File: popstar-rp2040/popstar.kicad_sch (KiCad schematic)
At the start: 31 parts, among them J1 JST SH 4-pin, J2 SWD, SW1 Boot, U1 RP2040, U2 XC6206PxxxMR, U3 SRV05-4, U4 W25Q128JVS, Y1 12MHz

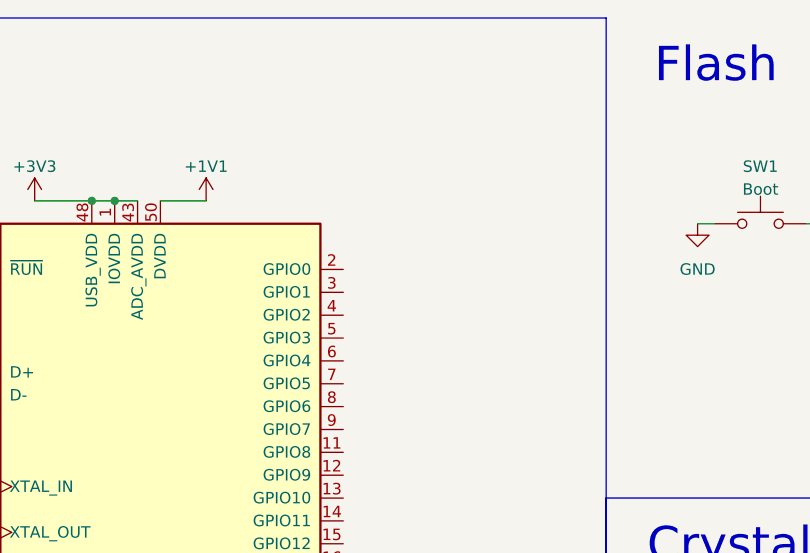
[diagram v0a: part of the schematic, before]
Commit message: Cleaned up LED schematic impl.
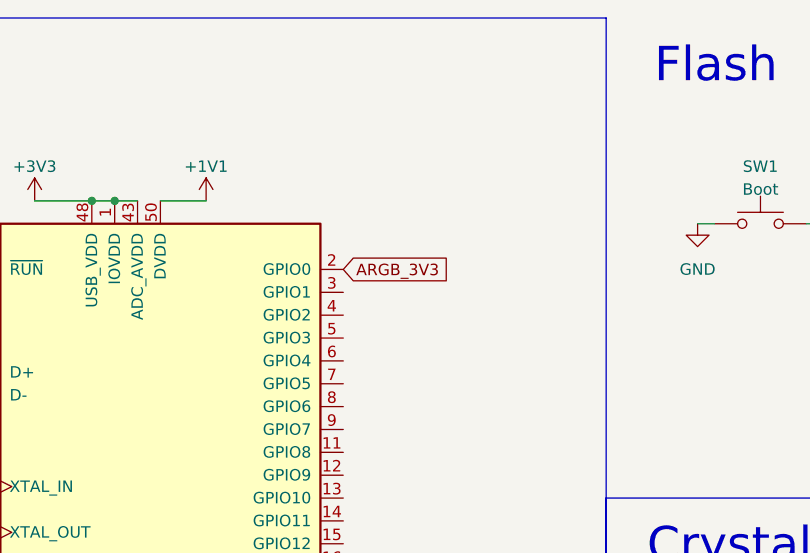
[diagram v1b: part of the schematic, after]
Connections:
- net ARGB_3V3: now reaches U1.2 (GPIO0)
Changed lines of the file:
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@@
+    )
+  )
+  (global_label "ARGB_3V3" (shape input) (at 85.09 40.64 0) (fields_autoplaced)
+    (effects (font (size 1.27 1.27)) (justify left))
+    (property "Intersheetrefs" "${INTERSHEET_REFS}" (at 97.3696 40.64 0)
+      (effects (font (size 1.27 1.27)) (justify left) hide)
     )
   )

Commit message: Added BOM spreadsheet, updated components with LCSC part numbers and footprints.
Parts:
- C1, C15, C16, C5: footprint (none) -> Capacitor_SMD:C_0402_1005Metric; LCSC (none) -> C52923
- C10, C11, C12, C17, C2, C3, C6, C9: footprint (none) -> Capacitor_SMD:C_0402_1005Metric; LCSC (none) -> C1525
- C13, C14: footprint (none) -> Capacitor_SMD:C_0402_1005Metric; LCSC (none) -> C1555
- C4: footprint (none) -> Capacitor_SMD:C_0402_1005Metric; LCSC (none) -> C15525
- C7, C8: footprint (none) -> Capacitor_SMD:C_0402_1005Metric; LCSC (none) -> 1525
- F1: footprint (none) -> Fuse:Fuse_1206_3216Metric; LCSC (none) -> C135342
- J1: LCSC (none) -> C160404
- J2, SW1: now left out of the parts list
- R1: footprint (none) -> Resistor_SMD:R_0402_1005Metric; LCSC (none) -> C25744
- R2, R3: footprint (none) -> Resistor_SMD:R_0603_1608Metric; LCSC (none) -> C25190
- R4, R5: footprint (none) -> Resistor_SMD:R_0402_1005Metric; LCSC (none) -> C11702
- U1: LCSC (none) -> C2040
- U2: LCSC (none) -> C5446
- U3: LCSC (none) -> C85364
- U4: LCSC (none) -> C97521
- Y1: footprint (none) -> Crystal:Crystal_SMD_3225-4Pin_3.2x2.5mm; LCSC (none) -> C9002

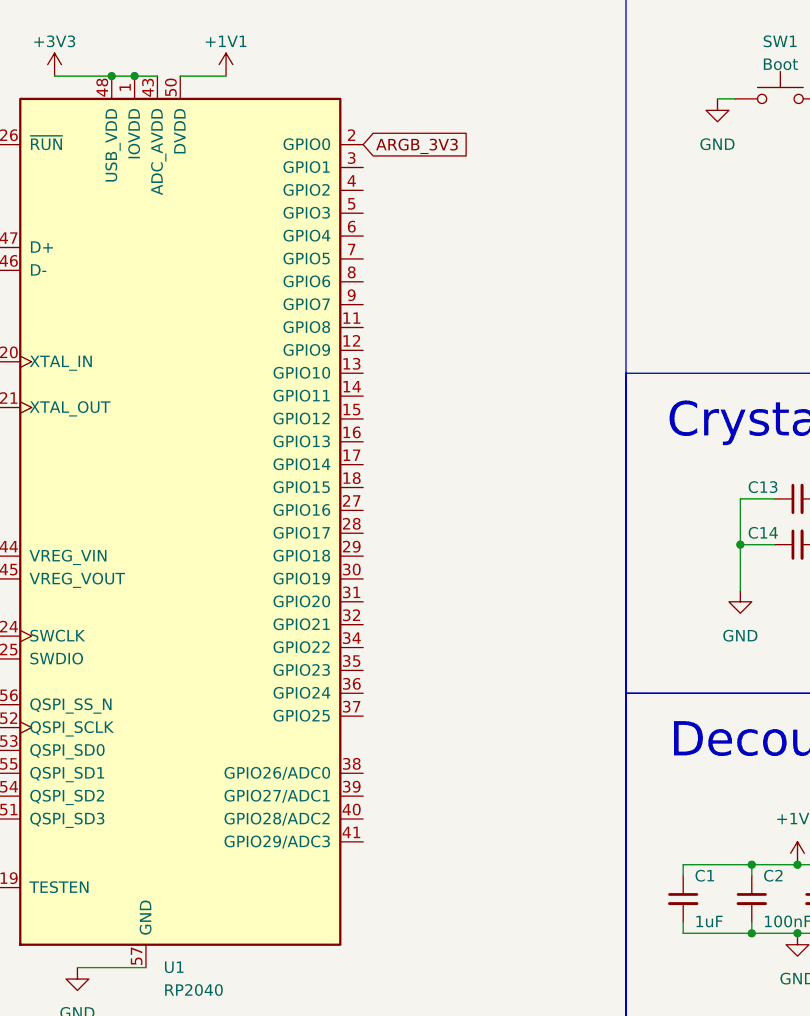
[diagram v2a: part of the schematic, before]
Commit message: Finished switch matrix, updated pin connections accordingly
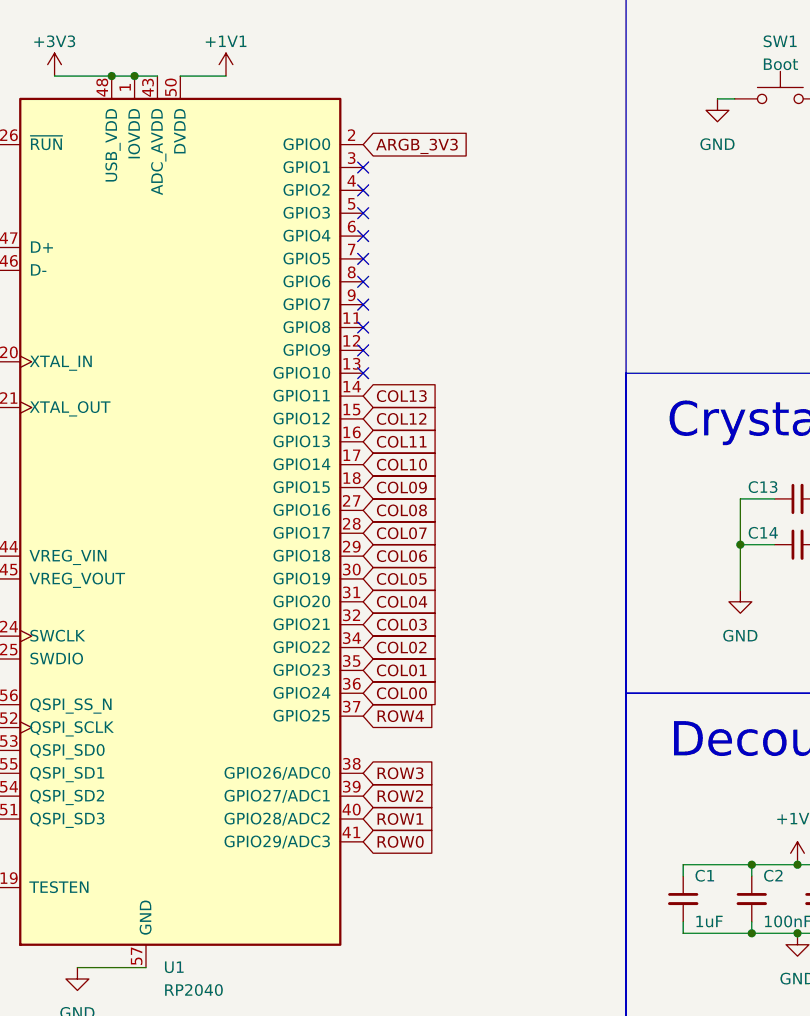
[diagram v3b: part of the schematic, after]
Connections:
- net COL13: now reaches U1.14 (GPIO11)
- net COL12: now reaches U1.15 (GPIO12)
- net COL11: now reaches U1.16 (GPIO13)
- net COL10: now reaches U1.17 (GPIO14)
- net COL09: now reaches U1.18 (GPIO15)
- net COL08: now reaches U1.27 (GPIO16)
- net COL07: now reaches U1.28 (GPIO17)
- net COL06: now reaches U1.29 (GPIO18)
- net COL05: now reaches U1.30 (GPIO19)
- net COL04: now reaches U1.31 (GPIO20)
- net COL03: now reaches U1.32 (GPIO21)
- net COL02: now reaches U1.34 (GPIO22)
- net COL01: now reaches U1.35 (GPIO23)
- net COL00: now reaches U1.36 (GPIO24)
- net ROW4: now reaches U1.37 (GPIO25)
- net ROW3: now reaches U1.38 (GPIO26/ADC0)
- net ROW2: now reaches U1.39 (GPIO27/ADC1)
- net ROW1: now reaches U1.40 (GPIO28/ADC2)
- net ROW0: now reaches U1.41 (GPIO29/ADC3)
- no-connect marks 2 -> 12
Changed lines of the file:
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@@
   (junction (at 173.99 120.65) (diameter 0) (color 0 0 0 0)
   )
+  (no_connect (at 85.09 55.88))
   (no_connect (at 248.92 36.83))
+  (no_connect (at 85.09 63.5))
+  (no_connect (at 85.09 66.04))
+  (no_connect (at 85.09 43.18))
+  (no_connect (at 85.09 48.26))
+  (no_connect (at 85.09 60.96))
+  (no_connect (at 85.09 58.42))
+  (no_connect (at 85.09 45.72))
+  (no_connect (at 85.09 50.8))
+  (no_connect (at 85.09 53.34))
   (no_connect (at 248.92 41.91))
   (wire (pts (xy 140.97 90.17) (xy 143.51 90.17))
@@
     )
   )
+  (global_label "ROW4" (shape input) (at 85.09 104.14 0) (fields_autoplaced)
+    (effects (font (size 1.27 1.27)) (justify left))
+    (property "Intersheetrefs" "${INTERSHEET_REFS}" (at 93.2572 104.14 0)
+      (effects (font (size 1.27 1.27)) (justify left) hide)
+    )
+  )
+  (global_label "COL00" (shape input) (at 85.09 101.6 0) (fields_autoplaced)
+    (effects (font (size 1.27 1.27)) (justify left))
+    (property "Intersheetrefs" "${INTERSHEET_REFS}" (at 94.0434 101.6 0)
+      (effects (font (size 1.27 1.27)) (justify left) hide)
+    )
+  )
   (global_label "QSPI_CLK" (shape input) (at 44.45 105.41 180) (fields_autoplaced)
     (effects (font (size 1.27 1.27)) (justify right))
@@
     )
   )
+  (global_label "COL07" (shape input) (at 85.09 83.82 0) (fields_autoplaced)
+    (effects (font (size 1.27 1.27)) (justify left))
+    (property "Intersheetrefs" "${INTERSHEET_REFS}" (at 94.0434 83.82 0)
+      (effects (font (size 1.27 1.27)) (justify left) hide)
+    )
+  )
   (global_label "SWD" (shape input) (at 262.89 88.9 0) (fields_autoplaced)
     (effects (font (size 1.27 1.27)) (justify left))
@@
     )
   )
+  (global_label "COL10" (shape input) (at 85.09 76.2 0) (fields_autoplaced)
+    (effects (font (size 1.27 1.27)) (justify left))
+    (property "Intersheetrefs" "${INTERSHEET_REFS}" (at 94.0434 76.2 0)
+      (effects (font (size 1.27 1.27)) (justify left) hide)
+    )
+  )
   (global_label "D_P" (shape input) (at 218.44 87.63 0) (fields_autoplaced)
     (effects (font (size 1.27 1.27)) (justify left))
@@
     )
   )
+  (global_label "ROW0" (shape input) (at 85.09 118.11 0) (fields_autoplaced)
+    (effects (font (size 1.27 1.27)) (justify left))
+    (property "Intersheetrefs" "${INTERSHEET_REFS}" (at 93.2572 118.11 0)
+      (effects (font (size 1.27 1.27)) (justify left) hide)
+    )
+  )
+  (global_label "COL13" (shape input) (at 85.09 68.58 0) (fields_autoplaced)
+    (effects (font (size 1.27 1.27)) (justify left))
+    (property "Intersheetrefs" "${INTERSHEET_REFS}" (at 94.0434 68.58 0)
+      (effects (font (size 1.27 1.27)) (justify left) hide)
+    )
+  )
+  (global_label "COL05" (shape input) (at 85.09 88.9 0) (fields_autoplaced)
+    (effects (font (size 1.27 1.27)) (justify left))
+    (property "Intersheetrefs" "${INTERSHEET_REFS}" (at 94.0434 88.9 0)
+      (effects (font (size 1.27 1.27)) (justify left) hide)
+    )
+  )
   (global_label "SWD" (shape input) (at 44.45 97.79 180) (fields_autoplaced)
     (effects (font (size 1.27 1.27)) (justify right))
@@
     )
   )
+  (global_label "ROW1" (shape input) (at 85.09 115.57 0) (fields_autoplaced)
+    (effects (font (size 1.27 1.27)) (justify left))
+    (property "Intersheetrefs" "${INTERSHEET_REFS}" (at 93.2572 115.57 0)
+      (effects (font (size 1.27 1.27)) (justify left) hide)
+    )
+  )
+  (global_label "COL06" (shape input) (at 85.09 86.36 0) (fields_autoplaced)
+    (effects (font (size 1.27 1.27)) (justify left))
+    (property "Intersheetrefs" "${INTERSHEET_REFS}" (at 94.0434 86.36 0)
+      (effects (font (size 1.27 1.27)) (justify left) hide)
+    )
+  )
   (global_label "SD3" (shape input) (at 44.45 115.57 180) (fields_autoplaced)
     (effects (font (size 1.27 1.27)) (justify right))
@@
     )
   )
+  (global_label "COL11" (shape input) (at 85.09 73.66 0) (fields_autoplaced)
+    (effects (font (size 1.27 1.27)) (justify left))
+    (property "Intersheetrefs" "${INTERSHEET_REFS}" (at 94.0434 73.66 0)
+      (effects (font (size 1.27 1.27)) (justify left) hide)
+    )
+  )
+  (global_label "COL12" (shape input) (at 85.09 71.12 0) (fields_autoplaced)
+    (effects (font (size 1.27 1.27)) (justify left))
+    (property "Intersheetrefs" "${INTERSHEET_REFS}" (at 94.0434 71.12 0)
+      (effects (font (size 1.27 1.27)) (justify left) hide)
+    )
+  )
   (global_label "SD2" (shape input) (at 182.245 41.91 0) (fields_autoplaced)
     (effects (font (size 1.27 1.27)) (justify left))
@@
     )
   )
+  (global_label "COL08" (shape input) (at 85.09 81.28 0) (fields_autoplaced)
+    (effects (font (size 1.27 1.27)) (justify left))
+    (property "Intersheetrefs" "${INTERSHEET_REFS}" (at 94.0434 81.28 0)
+      (effects (font (size 1.27 1.27)) (justify left) hide)
+    )
+  )
   (global_label "D_P" (shape input) (at 274.32 36.83 0) (fields_autoplaced)
     (effects (font (size 1.27 1.27)) (justify left))
@@
     )
   )
+  (global_label "COL04" (shape input) (at 85.09 91.44 0) (fields_autoplaced)
+    (effects (font (size 1.27 1.27)) (justify left))
+    (property "Intersheetrefs" "${INTERSHEET_REFS}" (at 94.0434 91.44 0)
+      (effects (font (size 1.27 1.27)) (justify left) hide)
+    )
+  )
+  (global_label "COL09" (shape input) (at 85.09 78.74 0) (fields_autoplaced)
+    (effects (font (size 1.27 1.27)) (justify left))
+    (property "Intersheetrefs" "${INTERSHEET_REFS}" (at 94.0434 78.74 0)
+      (effects (font (size 1.27 1.27)) (justify left) hide)
+    )
+  )
+  (global_label "ROW3" (shape input) (at 85.09 110.49 0) (fields_autoplaced)
+    (effects (font (size 1.27 1.27)) (justify left))
+    (property "Intersheetrefs" "${INTERSHEET_REFS}" (at 93.2572 110.49 0)
+      (effects (font (size 1.27 1.27)) (justify left) hide)
+    )
+  )
   (global_label "CS" (shape input) (at 44.45 102.87 180) (fields_autoplaced)
     (effects (font (size 1.27 1.27)) (justify right))
@@
     )
   )
+  (global_label "ROW2" (shape input) (at 85.09 113.03 0) (fields_autoplaced)
+    (effects (font (size 1.27 1.27)) (justify left))
+    (property "Intersheetrefs" "${INTERSHEET_REFS}" (at 93.2572 113.03 0)
+      (effects (font (size 1.27 1.27)) (justify left) hide)
+    )
+  )
   (global_label "SD0" (shape input) (at 182.245 34.29 0) (fields_autoplaced)
     (effects (font (size 1.27 1.27)) (justify left))
@@
     )
   )
+  (global_label "COL01" (shape input) (at 85.09 99.06 0) (fields_autoplaced)
+    (effects (font (size 1.27 1.27)) (justify left))
+    (property "Intersheetrefs" "${INTERSHEET_REFS}" (at 94.0434 99.06 0)
+      (effects (font (size 1.27 1.27)) (justify left) hide)
+    )
+  )
   (global_label "SWCLK" (shape input) (at 262.89 91.44 0) (fields_autoplaced)
     (effects (font (size 1.27 1.27)) (justify left))
@@
       (effects (font (size 1.27 1.27)) (justify left) hide)
     )
+  )
+  (global_label "COL03" (shape input) (at 85.09 93.98 0) (fields_autoplaced)
+    (effects (font (size 1.27 1.27)) (justify left))
+    (property "Intersheetrefs" "${INTERSHEET_REFS}" (at 94.0434 93.98 0)
+      (effects (font (size 1.27 1.27)) (justify left) hide)
+    )
+  )
+  (global_label "COL02" (shape input) (at 85.09 96.52 0) (fields_autoplaced)
+    (effects (font (size 1.27 1.27)) (justify left))
+    (property "Intersheetrefs" "${INTERSHEET_REFS}" (at 94.0434 96.52 0)
+      (effects (font (size 1.27 1.27)) (justify left) hide)
+    )

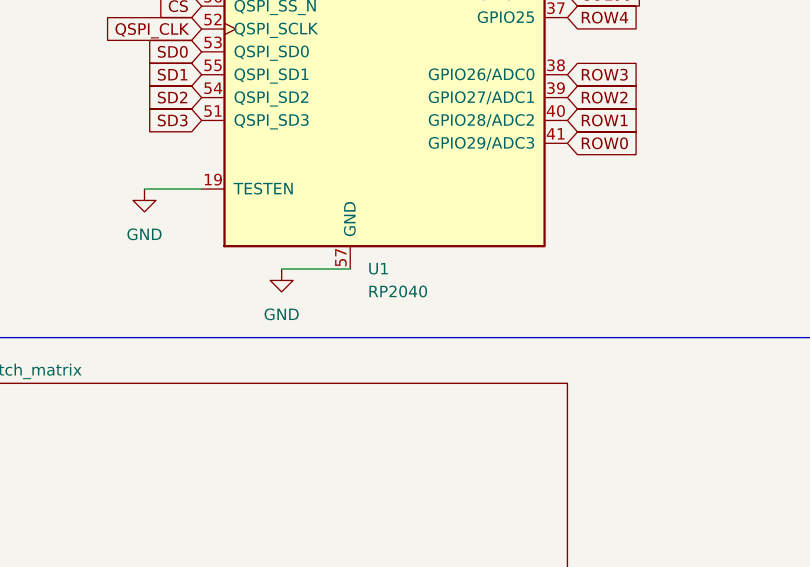
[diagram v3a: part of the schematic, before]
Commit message: Fixed missing footprints in schematic, added barfed out components in PCB editor. Properly connected sleep-lib symbol libraries into popstar project.
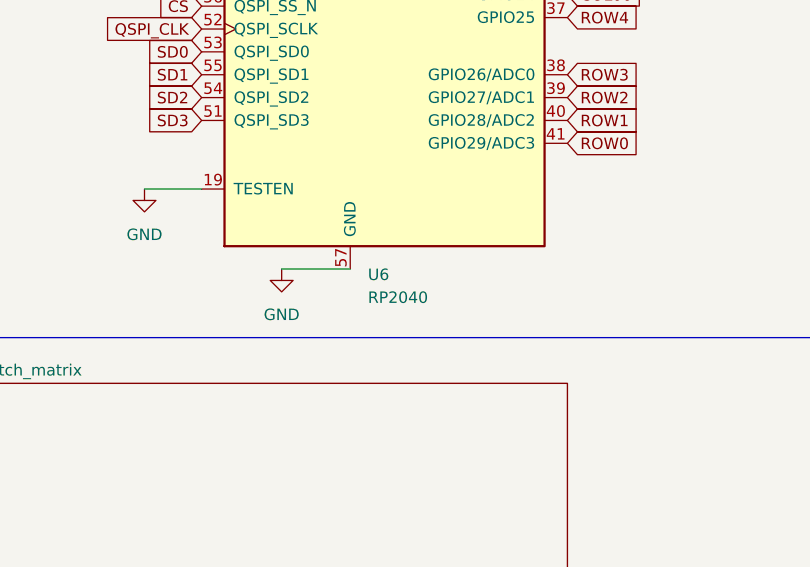
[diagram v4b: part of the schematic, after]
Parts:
- removed U1: RP2040, Sleep-Lib:RP2040-QFN-56, symbol Sleep-lib:RP2040
- added U6: RP2040, Sleep-Lib:RP2040-QFN-56, symbol Sleep-lib:RP2040
- J2: footprint (none) -> Connector_PinSocket_2.54mm:PinSocket_1x05_P2.54mm_Vertical
- SW1: footprint (none) -> Connector_PinSocket_2.54mm:PinSocket_1x02_P2.54mm_Vertical
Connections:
- net +1V1: now also U6.23 (DVDD), U6.45 (VREG_VOUT), U6.50 (DVDD)
- net +3V3: now also U6.1 (IOVDD), U6.10 (IOVDD), U6.22 (IOVDD), U6.33 (IOVDD), U6.42 (IOVDD), U6.43 (ADC_AVDD), U6.44 (VREG_VIN), U6.48 (USB_VDD), U6.49 (IOVDD)
- net ARGB_3V3: now also U6.2 (GPIO0)
- net COL00: now also U6.36 (GPIO24)
- net COL01: now also U6.35 (GPIO23)
- net COL02: now also U6.34 (GPIO22)
- net COL03: now also U6.32 (GPIO21)
- net COL04: now also U6.31 (GPIO20)
- net COL05: now also U6.30 (GPIO19)
- net COL06: now also U6.29 (GPIO18)
- net COL07: now also U6.28 (GPIO17)
- net COL08: now also U6.27 (GPIO16)
- net COL09: now also U6.18 (GPIO15)
- net COL10: now also U6.17 (GPIO14)
- net COL11: now also U6.16 (GPIO13)
- net COL12: now also U6.15 (GPIO12)
- net COL13: now also U6.14 (GPIO11)
- net CS: now also U6.56 (QSPI_SS_N)
- net D_+: now also U6.47 (D+)
- net D_-: now also U6.46 (D-)
- net GND: now also U6.19 (TESTEN), U6.57 (GND)
- net QSPI_CLK: now also U6.52 (QSPI_SCLK)
- net ROW0: now also U6.41 (GPIO29/ADC3)
- net ROW1: now also U6.40 (GPIO28/ADC2)
- net ROW2: now also U6.39 (GPIO27/ADC1)
- net ROW3: now also U6.38 (GPIO26/ADC0)
- net ROW4: now also U6.37 (GPIO25)
- net SD0: now also U6.53 (QSPI_SD0)
- net SD1: now also U6.55 (QSPI_SD1)
- net SD2: now also U6.54 (QSPI_SD2)
- net SD3: now also U6.51 (QSPI_SD3)
- net SWCLK: now also U6.24 (SWCLK)
- net SWD: now also U6.25 (SWDIO)
- net XTAL_IN: now also U6.20 (XTAL_IN)
- net XTAL_OUT: now also U6.21 (XTAL_OUT)
- net ~{RESET}: now also U6.26 (~{RUN})
